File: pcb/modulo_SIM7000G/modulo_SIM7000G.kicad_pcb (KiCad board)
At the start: 2 copper layers, 80 x 60 mm, 59 parts, among them J1 Conector Serial, J2 115Q-BCA0, J3 RF ANT, J4 GNSS ANT, J5 Jack-DC, Q1 NTE4153NT1G, Q2 NTE4153NT1G, Q3 NTE4153NT1G, U1 SIM7000G, U2 SN74LV1T34DCKR, U3 SN74LV1T34DCKR, U4 SN74LV1T34DCKR, U5 SN74LV1T34DCKR, U6 SN74LV1T34DCKR, U7 MIC29302WU, U8 LM1117-3.3

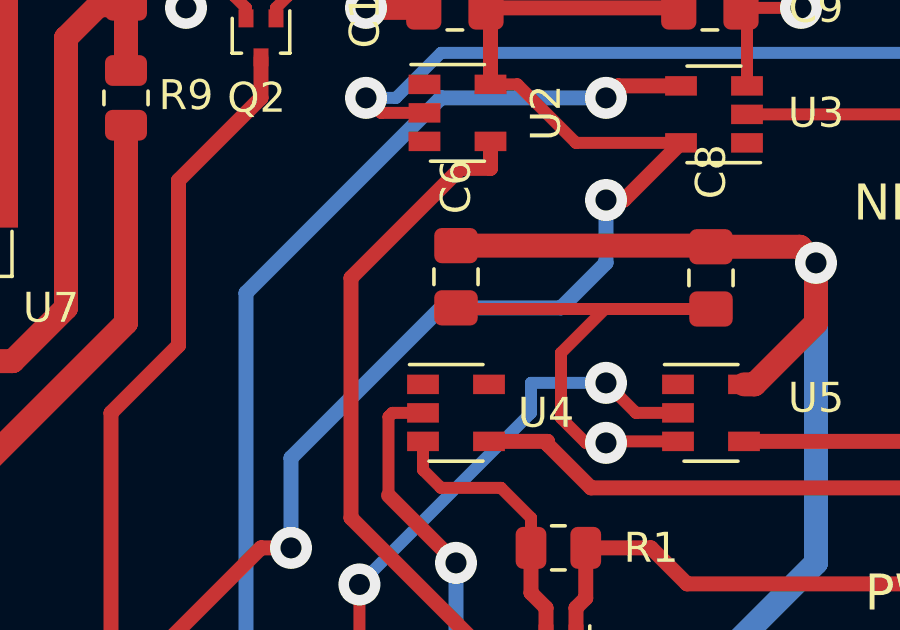
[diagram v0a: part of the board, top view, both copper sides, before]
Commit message: Se agrego los conectores de antenas. Faltasolucionar tema rutas relativas
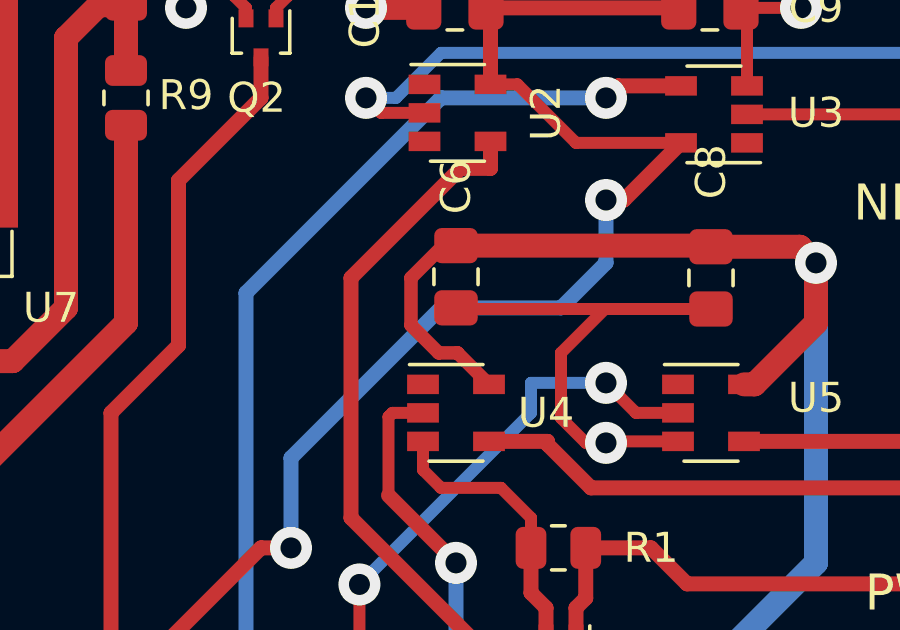
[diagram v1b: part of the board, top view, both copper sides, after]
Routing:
- net +3V3: track 98.4 -> 105.4 mm

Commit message: conectando nodos
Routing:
- net GND: track 259.6 -> 267.9 mm
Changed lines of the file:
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@@
     (thickness 1.6)
     (drawings 29)
-    (tracks 420)
+    (tracks 424)
     (zones 0)
     (modules 59)
@@
   )
   (setup
-    (last_trace_width 0.45)
+    (last_trace_width 0.4)
     (user_trace_width 0.4)
     (user_trace_width 0.5)
@@
   (via (at 146 130.5) (size 1.4) (drill 0.7) (layers F.Cu B.Cu) (net 1))
   (segment (start 146 133) (end 146 130.5) (width 0.4) (layer F.Cu) (net 1))
+  (segment (start 146.45 88.45) (end 143.45 88.45) (width 0.4) (layer F.Cu) (net 1))
+  (segment (start 143.45 88.45) (end 143 88) (width 0.4) (layer F.Cu) (net 1))
+  (segment (start 143 85.5) (end 144.5 84) (width 0.4) (layer F.Cu) (net 1))
+  (segment (start 143 88) (end 143 85.5) (width 0.4) (layer F.Cu) (net 1))
   (segment (start 159.5 129.0875) (end 159.5875 129) (width 0.8) (layer F.Cu) (net 2))
   (segment (start 159.5 131.5) (end 159.5 129.0875) (width 0.8) (layer F.Cu) (net 2))

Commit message: todo listo, menos el tema de las rutas relativas
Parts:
- moved J3 0.50 mm to (169.5, 114.5)
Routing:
- net Net-(J3-Pad1): track 17.4 -> 18.1 mm
- net Net-(C17-Pad2): track 11.6 -> 12.2 mm
- net Net-(C17-Pad1): track 10.7 -> 11.3 mm
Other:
- net class Microstrip added: clearance 0.4, trace_width 0.3, via_dia 1.4, via_drill 0.7
- rule trace_min: 0.4 -> 0.3
- board text added: "N° Capas = 2 FR4 TG 140ºC (mayer) Espesor entre capas: 1 mm Acabado: Espesor de cobre: 1 oz"
- board text added: "Pistas de impedancia 50 Ohms: 1.85mm. Calculado con KICAD."
- board text added: "Reglas de fabricacion (se agregaron algunas excepciones): Margen: 0,42mm Ancho de pista minimo: 0,45 mm Diametro de via minimo : 1,4/0.7 mm Grillas utilizadas: 1 mm 0,5 mm 0,1 mm para alineacion de componentes."
